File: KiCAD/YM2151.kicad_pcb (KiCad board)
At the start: 2 copper layers, 100 x 75 mm, 37 parts, among them J1 Audio-Jack-3_2Switches, P1 Power, P2 Analog, P3 Digital, P4 Digital, P5 CONN_01X01, P6 CONN_01X01, P7 CONN_01X01, P8 CONN_01X01, Q1 2SC1815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

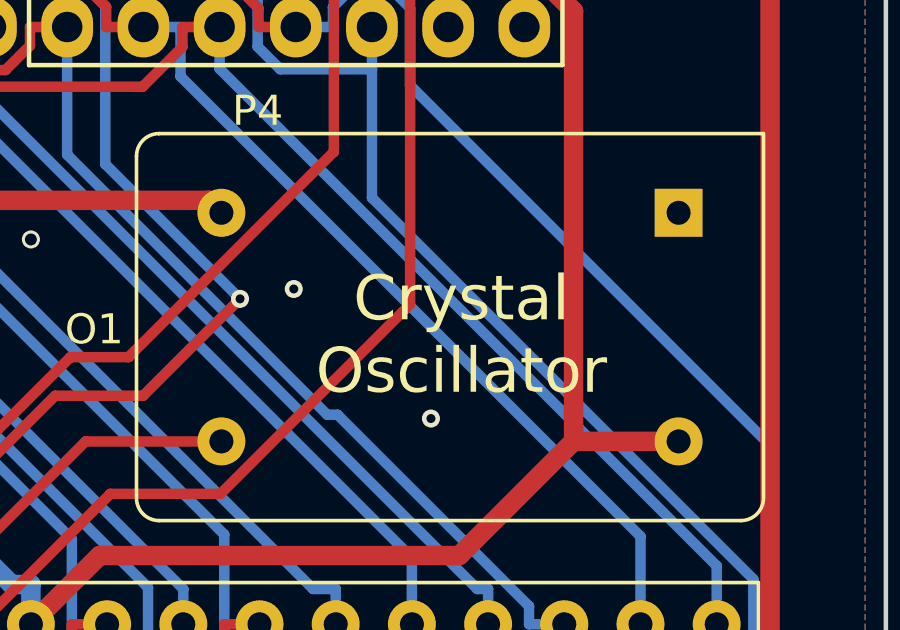
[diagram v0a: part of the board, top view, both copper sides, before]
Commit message: シルクパターン等整備
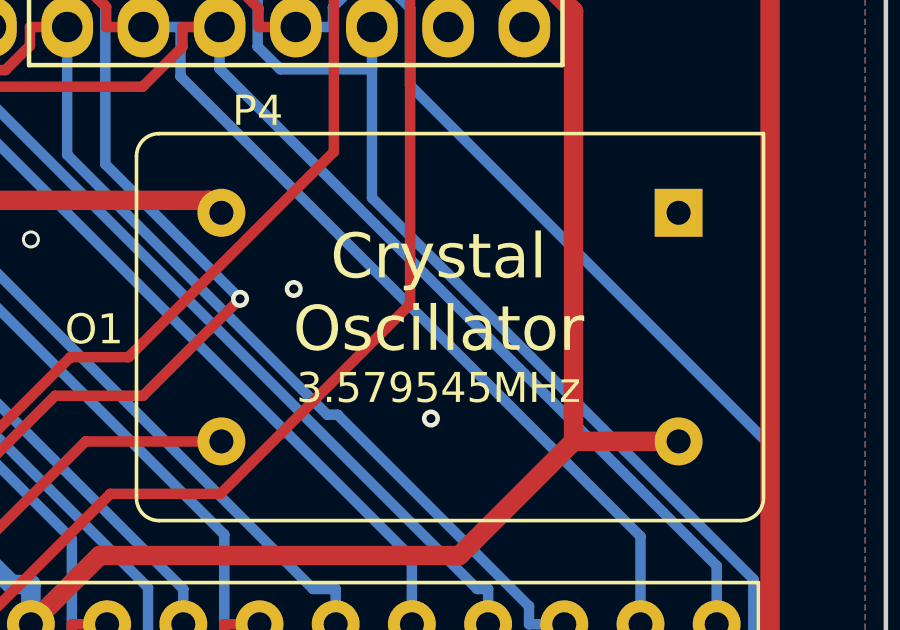
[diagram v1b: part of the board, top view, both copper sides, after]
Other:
- board text added: "3.579545MHz"
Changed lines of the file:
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@@
   (general
     (thickness 1.6)
-    (drawings 35)
+    (drawings 36)
     (tracks 653)
     (zones 0)
@@
     )
   )
+  (gr_text 3.579545MHz (at 171.638 87.6) (layer F.SilkS)
+    (effects (font (size 1 1) (thickness 0.15)))
+  )
   (gr_text 3 (at 174.94 58.39) (layer F.SilkS)
     (effects (font (size 1 1) (thickness 0.15)))
@@
     (effects (font (size 1 1) (thickness 0.2)))
   )
-  (gr_text "Crystal\nOscillator" (at 172.4 85.822) (layer F.SilkS)
+  (gr_text "Crystal\nOscillator" (at 171.638 84.425) (layer F.SilkS)
     (effects (font (size 1.5 1.5) (thickness 0.3)))
   )
